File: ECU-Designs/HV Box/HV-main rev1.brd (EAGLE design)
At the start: 196.1 x 63.5 mm, 68 parts, among them IC2 MCP6002SOIC, IC3 MCP6002SOIC

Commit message: Update nanofit pin numbers, add board files ready to send off
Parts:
- R26: value 1.8k -> 1k
- R5: value (none) -> 100
- R6, R7: value (none) -> 10k
- moved DISCH- 2.54 mm to (177.8, 45.3)
- moved HV-UNFUSED 2.54 mm to (190.2, 45.5)
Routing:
- net DISCHARGE3: track 24.5 -> 25.5 mm
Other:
- board text added: "Low Voltage Side"

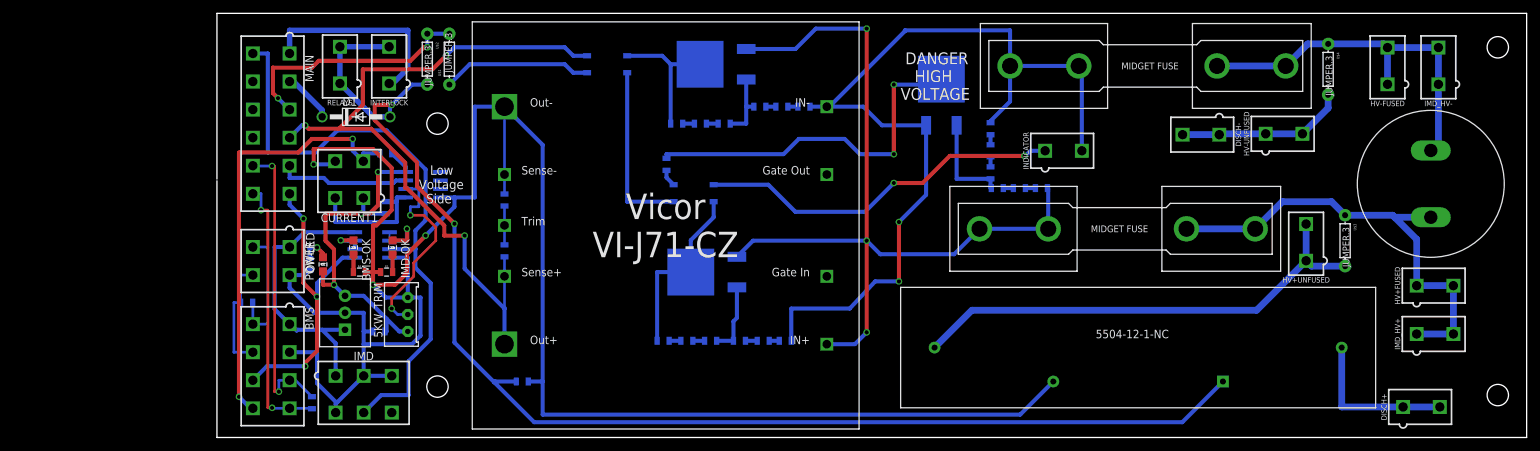
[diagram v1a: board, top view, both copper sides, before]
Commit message: Move files, upload final designs with logos, update jeff bms layout for rules compliance
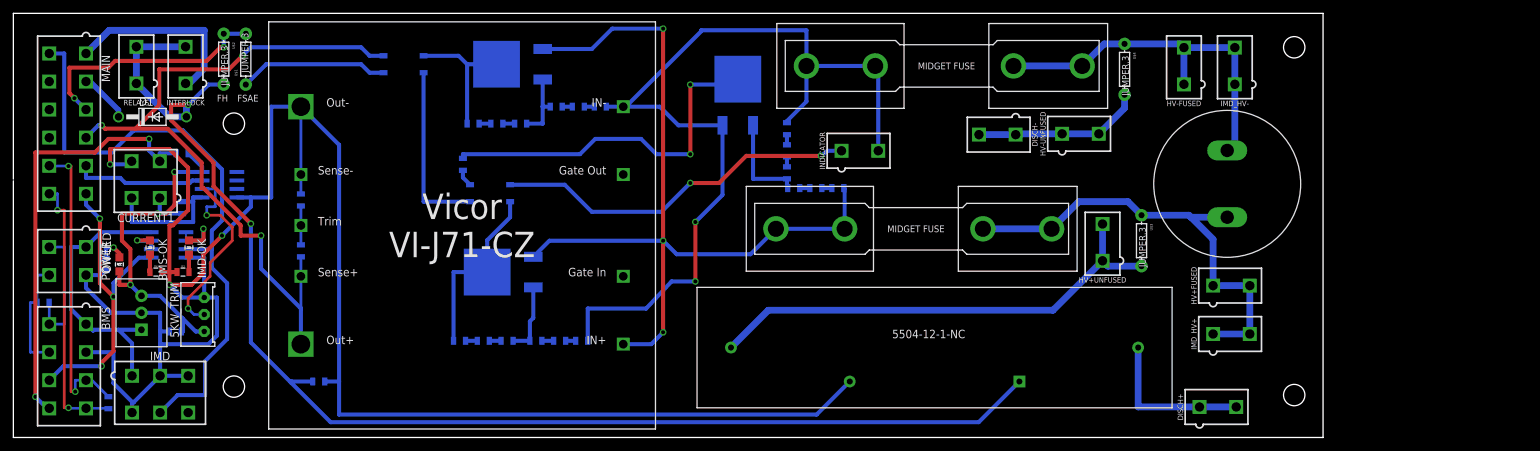
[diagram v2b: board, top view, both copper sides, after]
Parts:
- BMS: value MINIFIT_5566-8 -> (none)
- IMD: value CONNECTOR-6 -> (none)
- IMD_HV+, IMD_HV-: value CONNECTOR-2 -> (none)
- INDICATOR, INTERLOCK, RELAYS: value MINIFIT_5566-2 -> (none)
- moved C1 30.5 mm to (181.7, 38.0)
- moved DISCH- 30.5 mm to (147.3, 45.3)
- moved HV-FUSED 30.5 mm to (175.3, 55.6)
- moved HV-UNFUSED 30.5 mm to (159.8, 45.5)
- moved IMD_HV- 30.5 mm to (182.9, 55.6)
- moved R15 30.5 mm to (120.1, 37.3)
- moved U$12 30.5 mm to (102.4, 22.5)
- moved AI_SSR 30.5 mm to (71.4, 36.6)
- moved D2 30.5 mm to (45.7, 8.38)
- moved HV_REG2 30.5 mm to (77.9, 24.8)
- moved INDICATOR 30.5 mm to (126.7, 42.9)
- moved INTERLOCK 30.5 mm to (25.8, 55.8)
- moved R10 30.5 mm to (81.3, 49.5)
- moved R11 30.5 mm to (75.9, 47.0)
- moved R12 30.5 mm to (72.4, 47.0)
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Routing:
- net SHUTDOWN6: track 30.6 -> 28.6 mm
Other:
- board text added: "+"
- board text added: "-"
- board text added: "FH"
- board text added: "FH JUMP"
- board text added: "FSAE"
